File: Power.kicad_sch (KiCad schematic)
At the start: 0 parts

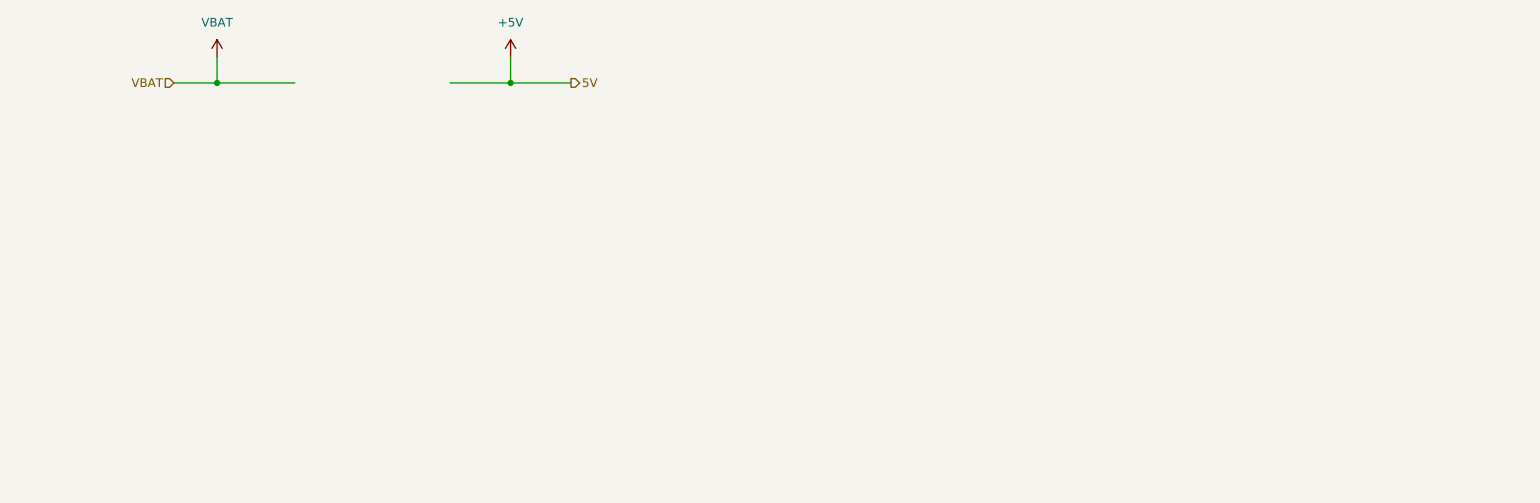
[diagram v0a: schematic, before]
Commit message: drew buck circuit
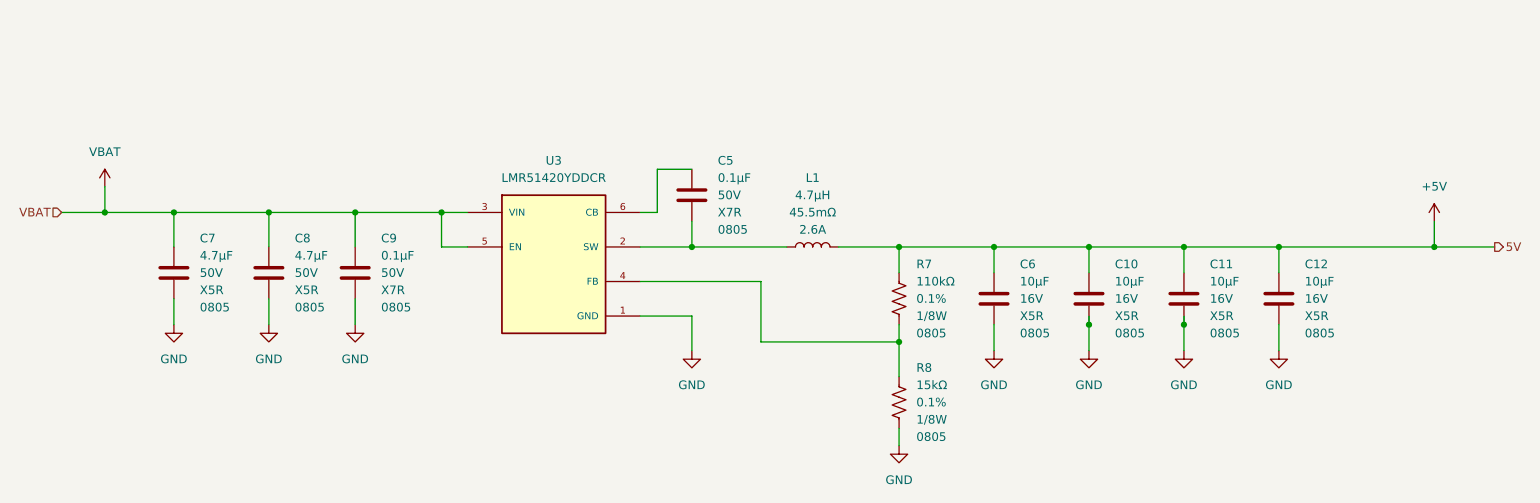
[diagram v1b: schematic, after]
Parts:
- added C10, C11, C12, C6: GRM21BR61C106KE15K, Capacitor_SMD:C_0805_2012Metric_Pad1.18x1.45mm_HandSolder, symbol Capacitors_MLCC:GRM21BR61C106KE15K
- added C5, C9: CL21B104KBCNNNC, Capacitor_SMD:C_0805_2012Metric_Pad1.18x1.45mm_HandSolder, symbol Capacitors_MLCC:CL21B104KBCNNNC
- added C7, C8: GRM21BR61H475KE51L, Capacitor_SMD:C_0805_2012Metric_Pad1.18x1.45mm_HandSolder, symbol Capacitors_MLCC:GRM21BR61H475KE51L
- added L1: NRS5030T4R7MMGJV, Inductor_SMD:L_Taiyo-Yuden_NRS5030T4R7MMGJV, symbol Inductors:NRS5030T4R7MMGJV
- added R7: ERA-6AEB114V, Resistor_SMD:R_0805_2012Metric_Pad1.20x1.40mm_HandSolder, symbol Resistors:ERA-6AEB114V
- added R8: RT0805BRD0715KL, Resistor_SMD:R_0805_2012Metric_Pad1.20x1.40mm_HandSolder, symbol Resistors:RT0805BRD0715KL
- added U3: LMR51420YDDCR, Package_TO_SOT_SMD:SOT-23-6_LMR51420YDDCR, symbol Regulator_Switching:LMR51420YDDCR
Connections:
- net +5V: now also C10.1, C11.1, C12.1, C6.1, L1.2, R7.1
- net VBAT: now also C7.1, C8.1, C9.1, U3.3 (VIN), U3.5 (EN)
- new net: R7.2, R8.1, U3.4 (FB)
- new net: C5.1, U3.6 (CB)
- new net: C5.2, L1.1, U3.2 (SW)
- new net GND: C10.2, C11.2, C12.2, C6.2, C7.2, C8.2, C9.2, R8.2, U3.1 (GND)

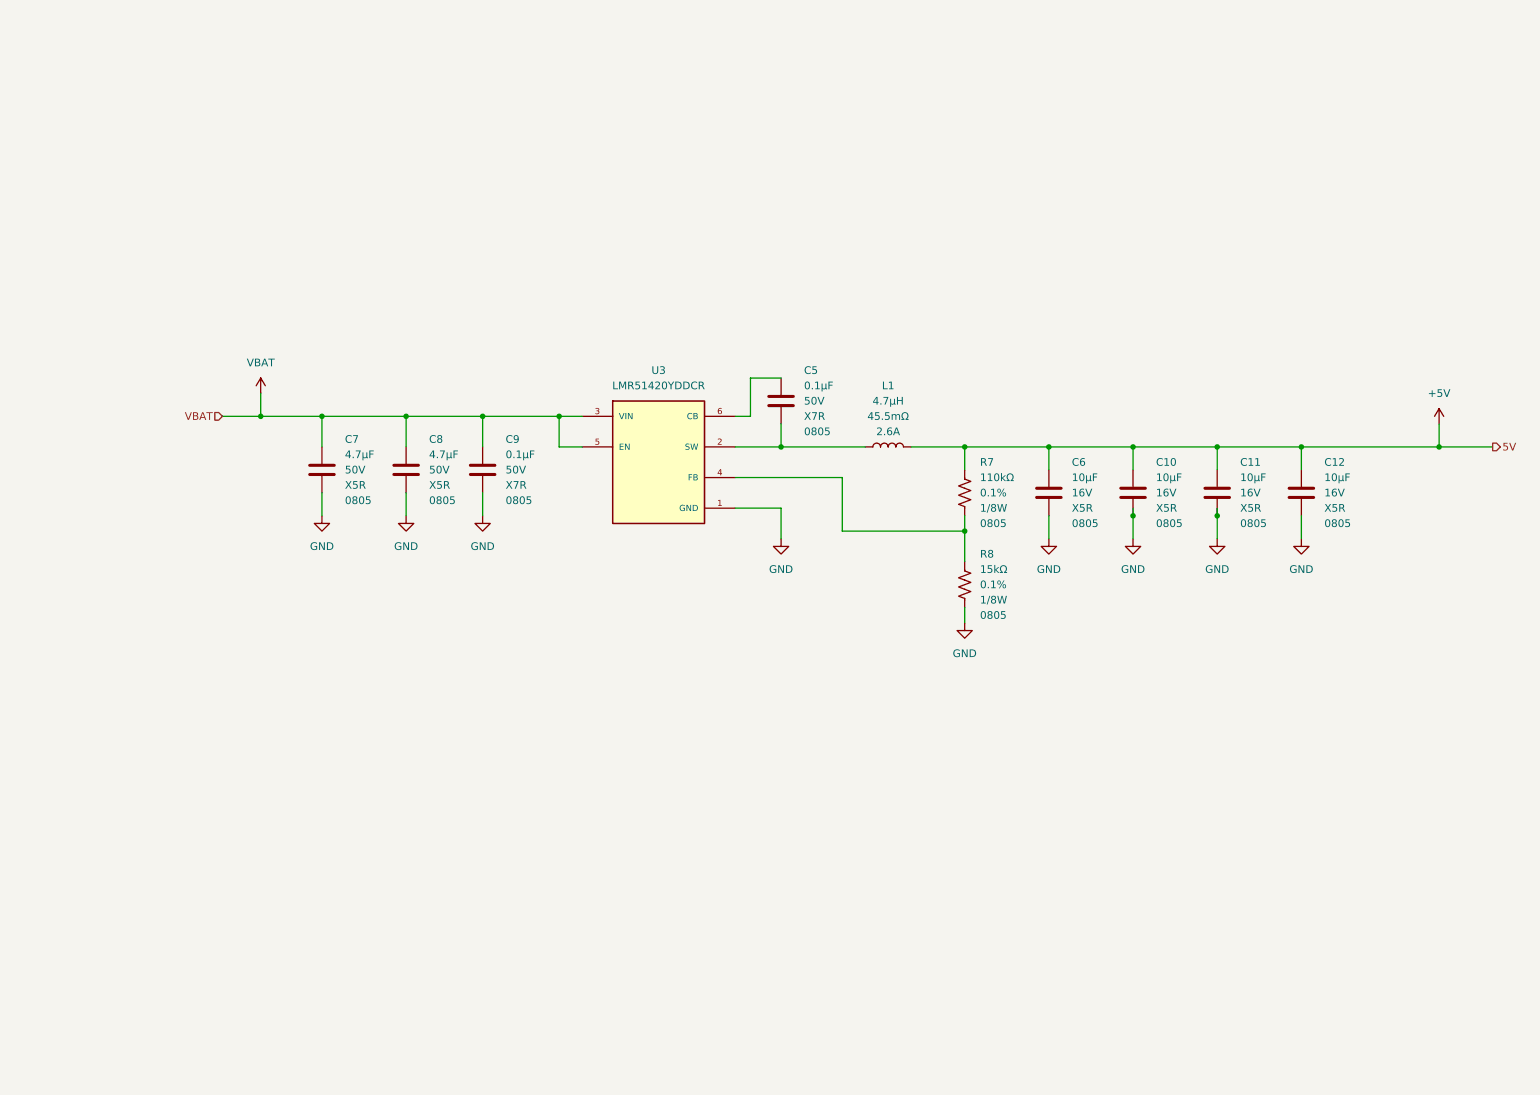
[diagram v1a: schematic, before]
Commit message: added CMC, TVS diode, electrolytic cap at buck input to improve inrush current effects
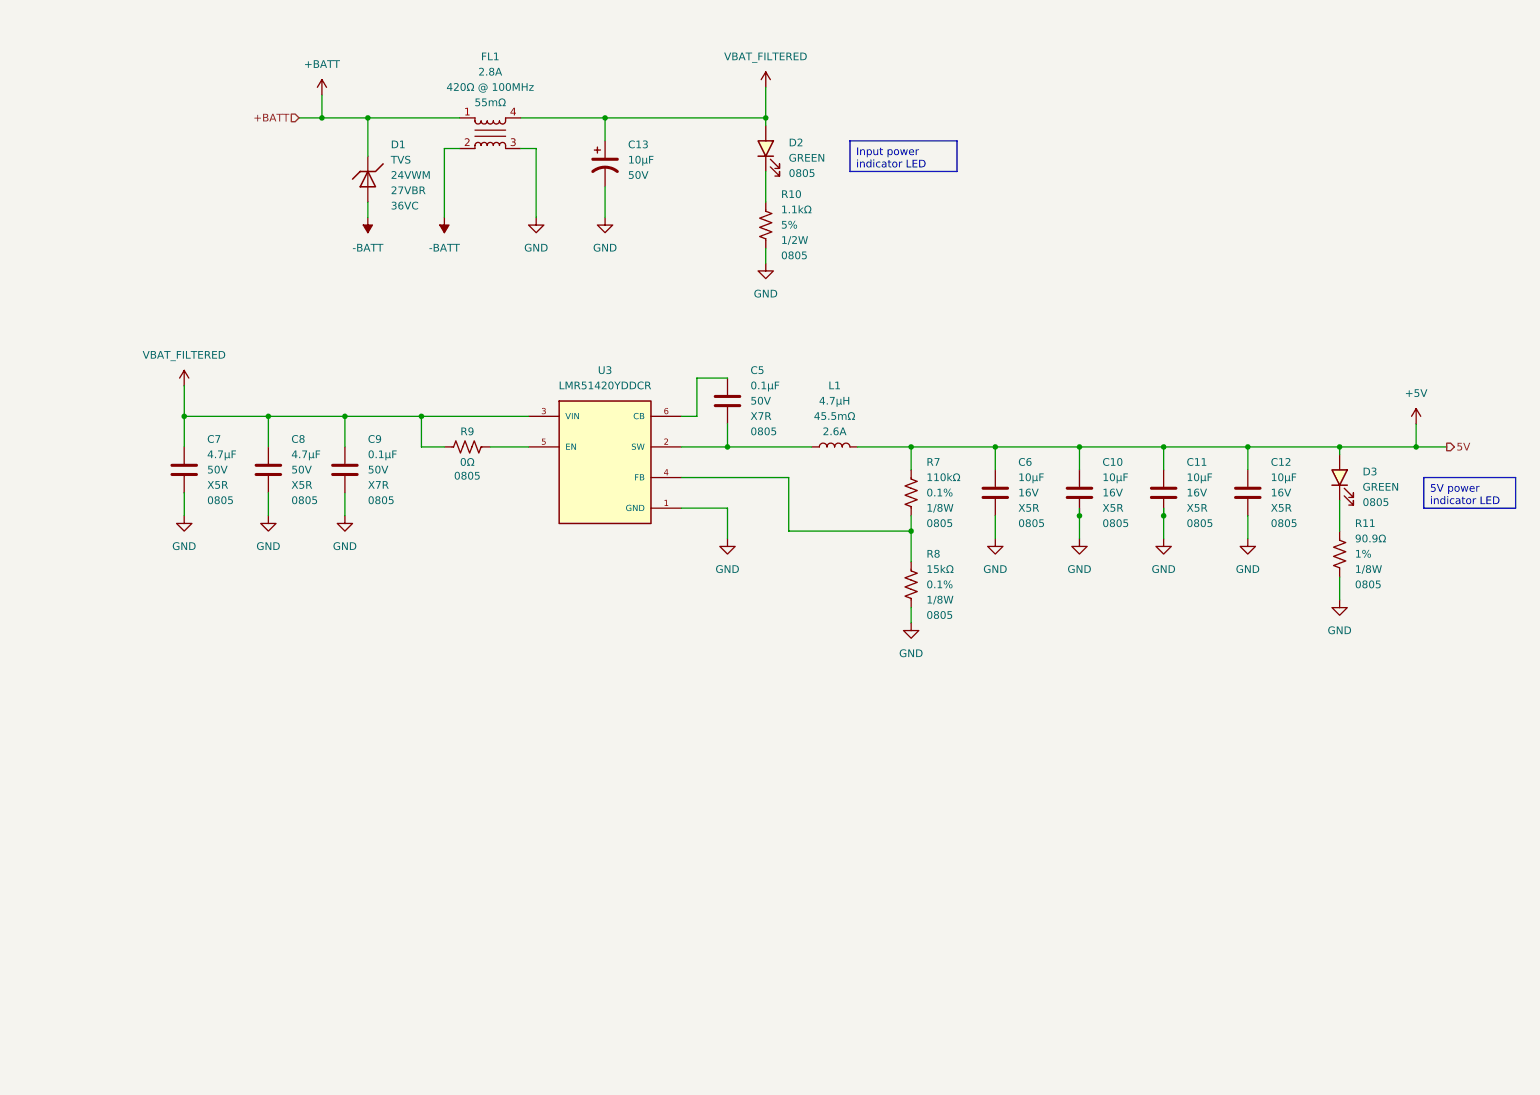
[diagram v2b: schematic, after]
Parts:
- added C13: 865080642006, Capacitor_SMD:865080642006, symbol Capacitor_Polarized:865080642006
- added D1: D24V0S1U2TQ-7, Diode_SMD:D_SOD-523, symbol Diode:D24V0S1U2TQ-7
- added D2, D3: 150080GS75000, LED_SMD:LED_0805_2012Metric_Pad1.15x1.40mm_HandSolder, symbol LED:150080GS75000
- added FL1: ACM4520-421-2P-T000, Inductor_SMD:L_CommonModeChoke_TDK_ACM4520-421-2P-T000, symbol Filter:CMC_TDK_ACM4520-421-2P-T000
- added R10: ERJ-P06J112V, Resistor_SMD:R_0805_2012Metric_Pad1.20x1.40mm_HandSolder, symbol Resistors:ERJ-P06J112V
- added R11: RC0805FR-0790R9L, Resistor_SMD:R_0805_2012Metric_Pad1.20x1.40mm_HandSolder, symbol Resistors:RC0805FR-0790R9L
- added R9: RC0805JR-070RL, Resistor_SMD:R_0805_2012Metric_Pad1.20x1.40mm_HandSolder, symbol Resistors:RC0805JR-070RL
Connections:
- net +5V: now also D3.2 (A)
- net GND: now also C13.2, FL1.3, R10.2, R11.2
- net VBAT renamed VBAT_FILTERED
- net VBAT_FILTERED: now also C13.1, D2.2 (A), FL1.4, R9.1; no longer U3.5 (EN)
- new net: D2.1 (K), R10.1
- new net: D3.1 (K), R11.1
- new net: R9.2, U3.5 (EN)
- new net +BATT: D1.1 (C), FL1.1
- new net -BATT: D1.2 (A), FL1.2
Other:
- moved on the sheet: C10, C11, C12, C5, C6, C7, C8, C9, L1, R7, R8, U3

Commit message: Added solenoid driver circuit
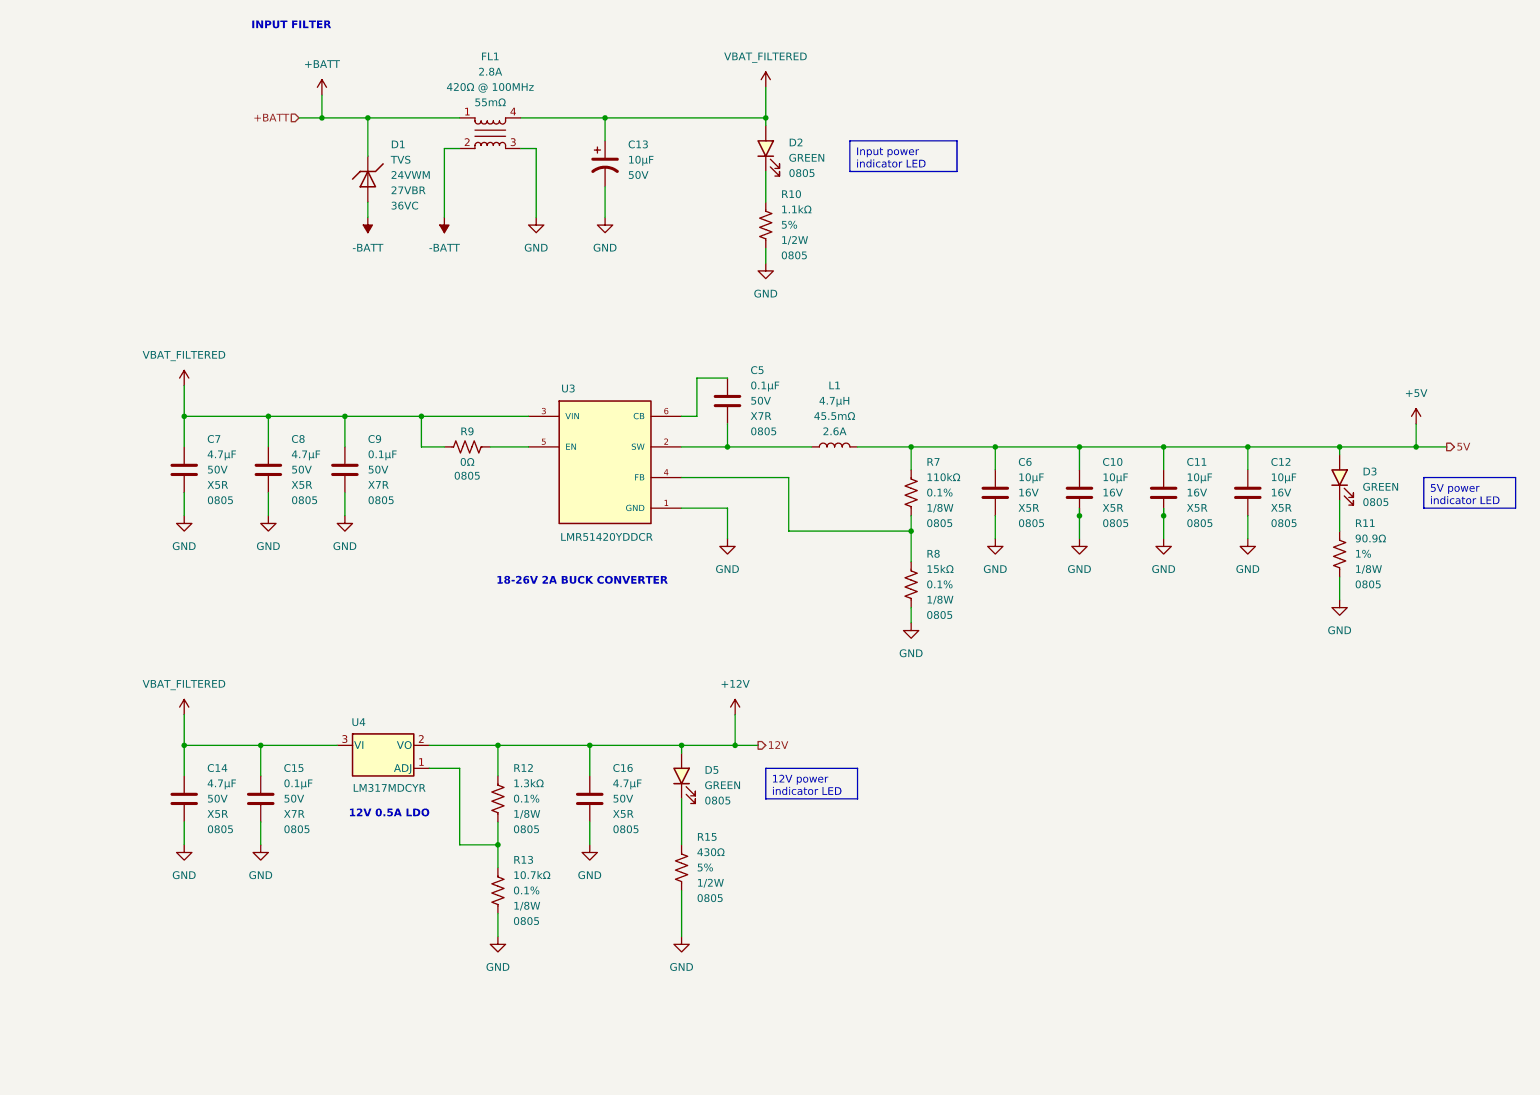
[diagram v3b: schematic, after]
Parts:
- added C14, C16: GRM21BR61H475KE51L, Capacitor_SMD:C_0805_2012Metric_Pad1.18x1.45mm_HandSolder, symbol Capacitors_MLCC:GRM21BR61H475KE51L
- added C15: CL21B104KBCNNNC, Capacitor_SMD:C_0805_2012Metric_Pad1.18x1.45mm_HandSolder, symbol Capacitors_MLCC:CL21B104KBCNNNC
- added D5: 150080GS75000, LED_SMD:LED_0805_2012Metric_Pad1.15x1.40mm_HandSolder, symbol LED:150080GS75000
- added R12: RT0805BRD071K3L, Resistor_SMD:R_0805_2012Metric_Pad1.20x1.40mm_HandSolder, symbol Resistors:RT0805BRD071K3L
- added R13: RT0805BRD0710K7L, Resistor_SMD:R_0805_2012Metric_Pad1.20x1.40mm_HandSolder, symbol Resistors:RT0805BRD0710K7L
- added R15: ERJ-P06J112V, Resistor_SMD:R_0805_2012Metric_Pad1.20x1.40mm_HandSolder, symbol Resistors:ERJ-P06J431V
- added U4: LM317MDCYR, Package_TO_SOT_SMD:SOT-223-3_TabPin2, symbol Regulator_Linear:LM317MDCYR
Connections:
- net GND: now also C14.2, C15.2, C16.2, R13.2, R15.2
- net VBAT_FILTERED: now also C14.1, C15.1, U4.3 (VI)
- new net: D5.1 (K), R15.1
- new net: R12.2, R13.1, U4.1 (ADJ)
- new net +12V: C16.1, D5.2 (A), R12.1, U4.2 (VO)
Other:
- note added: "12V 0.5A LDO"
- note added: "18-26V 2A BUCK CONVERTER"
- note added: "INPUT FILTER"

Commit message: 1st round of rough component placement
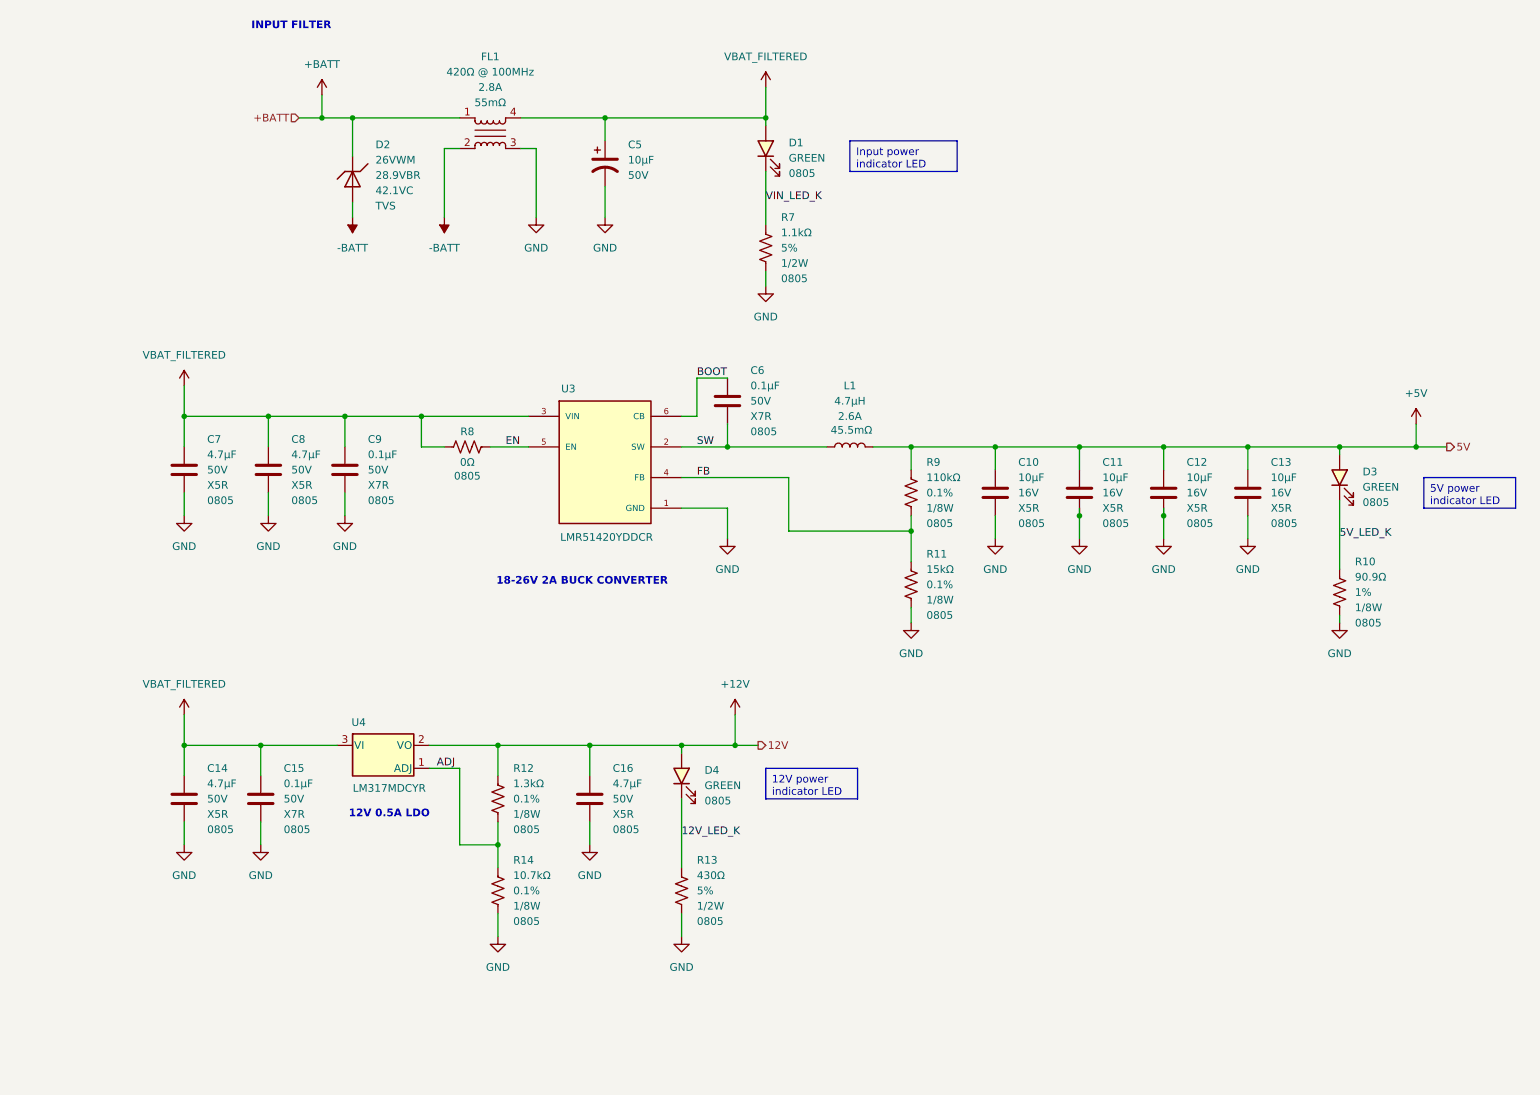
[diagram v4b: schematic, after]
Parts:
- removed D1: D24V0S1U2TQ-7, Diode_SMD:D_SOD-523, symbol Diode:D24V0S1U2TQ-7
- added D2: SMAJ26A-13-F, Diode_SMD:D_SMAJ26A-13-F, symbol Diode:SMAJ26A-13-F
- U4: footprint Package_TO_SOT_SMD:SOT-223-3_TabPin2 -> Package_TO_SOT_SMD:SOT-223-3_TabPin2_LM317MDCYR
- renumbered C6 to C10, C10 to C11, C11 to C12, C12 to C13, C13 to C5, C5 to C6, D2 to D1, D5 to D4, R11 to R10, R8 to R11, R15 to R13, R13 to R14, R10 to R7, R9 to R8, R7 to R9
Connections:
- net +BATT: now also D2.1 (C)
- net -BATT: now also D2.2 (A)
- net VIN_LED_K: now reaches D1.1 (K), R7.1
- net FB: now reaches R11.1, R9.2, U3.4 (FB)
- net 12V_LED_K: now reaches D4.1 (K), R13.1
- net 5V_LED_K: now reaches D3.1 (K), R10.1
- net BOOT: now reaches C6.1, U3.6 (CB)
- net SW: now reaches C6.2, L1.1, U3.2 (SW)
- net EN: now reaches R8.2, U3.5 (EN)
- net ADJ: now reaches R12.2, R14.1, U4.1 (ADJ)
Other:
- moved on the sheet: L1, R10, R13, R7
